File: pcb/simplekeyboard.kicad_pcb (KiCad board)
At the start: 2 copper layers, 288.1 x 97.6 mm, 164 parts, among them J1 USB_C_Receptacle_USB2.0_16P, J2 Conn_ARM_JTAG_SWD_10, SW1 SW_Push, SW10 SW_Push, SW11 SW_Push, SW12 SW_Push, SW13 SW_Push, SW14 SW_Push, SW15 SW_Push, SW16 SW_Push, SW17 SW_Push, SW18 SW_Push, SW19 SW_Push, SW2 SW_Push, SW20 SW_Push, SW21 SW_Push, SW22 SW_Push, SW23 SW_Push, SW24 SW_Push, SW25 SW_Push, SW26 SW_Push, SW27 SW_Push, SW28 SW_Push, SW29 SW_Push, SW3 SW_Push, SW30 SW_Push, SW31 SW_Push, SW32 SW_Push, SW33 SW_Push, SW34 SW_Push, SW35 SW_Push, SW36 SW_Push, SW37 SW_Push, SW38 SW_Push, SW39 SW_Push, SW4 SW_Push, SW40 SW_Push, SW41 SW_Push, SW42 SW_Push, SW43 SW_Push, SW44 SW_Push, SW45 SW_Push, SW46 SW_Push, SW47 SW_Push, SW48 SW_Push, SW49 SW_Push, SW5 SW_Push, SW50 SW_Push, SW51 SW_Push, SW52 SW_Push, SW53 SW_Push, SW54 SW_Push, SW55 SW_Push, SW56 SW_Push, SW57 SW_Push, SW58 SW_Push, SW59 SW_Push, SW6 SW_Push, SW60 SW_Push, SW61 SW_Push, SW62 SW_SPDT, SW63 SW_Push, SW7 SW_Push, SW8 SW_Push, SW9 SW_Push, U1 STM32F072CBT6, U2 USBLC6-2SC6, U3 LD39050PU33R, U4 MCP23017_SO, U5 MCP23008-xSO

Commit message: Cleanup silkscreen
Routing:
- net GND: track 65.4 -> 68.7 mm, vias 88 -> 91
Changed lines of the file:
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@@
 			(at 0 -4.5 0)
 			(layer "F.SilkS")
+			(hide yes)
 			(effects
 				(font
@@
 		)
 		(fp_text user "${REFERENCE}"
+			(at 0 -4.75 0)
+			(layer "F.Fab")
+			(effects
+				(font
+					(size 1 1)
+					(thickness 0.15)
+				)
+			)
+		)
+		(fp_text user "${REFERENCE}"
 			(at 0 0 0)
 			(layer "F.Fab")
@@
 			(at 0 -3.5 0)
 			(layer "F.SilkS")
+			(hide yes)
 			(effects
 				(font
@@
 			(at 0 -3.5 0)
 			(layer "F.SilkS")
+			(hide yes)
 			(effects
 				(font
@@
 			(at 0 -4.5 0)
 			(layer "F.SilkS")
+			(hide yes)
 			(effects
 				(font
@@
 			(at 0 -4.5 0)
 			(layer "F.SilkS")
+			(hide yes)
 			(effects
 				(font
@@
 			(at 0 -4.5 0)
 			(layer "F.SilkS")
+			(hide yes)
 			(effects
 				(font
@@
 		(tags "capacitor")
 		(property "Reference" "C7"
-			(at 0 1.43 0)
+			(at 0 -1.6 0)
 			(layer "B.SilkS")
 			(effects
@@
 		(tags "resistor")
 		(property "Reference" "R1"
-			(at 0 1.65 180)
+			(at -2.6 0 180)
 			(layer "B.SilkS")
 			(effects
@@
 		(tags "capacitor")
 		(property "Reference" "C2"
-			(at 0 1.43 0)
+			(at -0.6 1.4 0)
 			(layer "B.SilkS")
 			(effects
@@
 		(tags "capacitor")
 		(property "Reference" "C9"
-			(at 0 1.43 0)
+			(at 0 -1.4 0)
 			(layer "B.SilkS")
 			(effects
@@
 		(tags "capacitor")
 		(property "Reference" "C13"
-			(at 0 1.43 90)
+			(at -3.05 0 90)
 			(layer "B.SilkS")
 			(effects
@@
 		(tags "capacitor")
 		(property "Reference" "C12"
-			(at 0 1.43 90)
+			(at -3.05 0 90)
 			(layer "B.SilkS")
 			(effects
@@
 		(tags "capacitor")
 		(property "Reference" "C10"
-			(at 0 1.43 0)
+			(at 0.7 1.43 0)
 			(layer "B.SilkS")
 			(effects
@@
 		(tags "LD39050PU33R ")
 		(property "Reference" "U3"
-			(at 0 -2.600001 270)
+			(at -0.540625 -2.878125 0)
 			(unlocked yes)
 			(layer "B.SilkS")
@@
 		(tags "SOD-123")
 		(property "Reference" "D62"
-			(at 0 -1.85 0)
+			(at 0 1.6875 0)
 			(layer "B.SilkS")
 			(effects
@@
 		(tags "SOT TO_SOT_SMD")
 		(property "Reference" "U2"
-			(at 0 2.4 90)
+			(at 0 -2.578125 90)
 			(layer "B.SilkS")
 			(effects
@@
 		(tags "capacitor")
 		(property "Reference" "C8"
-			(at 0 1.43 0)
+			(at 0 -1.4 0)
 			(layer "B.SilkS")
 			(effects
@@
 		(tags "resistor")
 		(property "Reference" "R7"
-			(at 0 1.43 0)
+			(at -2.4 0 0)
 			(layer "B.SilkS")
 			(effects
@@
 		(tags "resistor")
 		(property "Reference" "R5"
-			(at 0 1.43 90)
+			(at -2.6 0 90)
 			(layer "B.SilkS")
 			(effects
@@
 		(tags "SOD-123")
 		(property "Reference" "D29"
-			(at 0 2 90)
+			(at 0 -1.8 90)
 			(layer "B.SilkS")
 			(effects
@@
 		(tags "resistor")
 		(property "Reference" "R2"
-			(at 0 1.65 180)
+			(at -2.6 0 180)
 			(layer "B.SilkS")
 			(effects
@@
 		(tags "resistor")
 		(property "Reference" "R10"
-			(at 0 1.43 90)
+			(at -3.05 0 90)
 			(layer "B.SilkS")
 			(effects
@@
 		(tags "resistor")
 		(property "Reference" "R9"
-			(at 0 1.43 90)
+			(at -2.6 0 90)
 			(layer "B.SilkS")
 			(effects
@@
 		(tags "resistor")
 		(property "Reference" "R4"
-			(at 0 1.43 90)
+			(at -2.6 0 90)
 			(layer "B.SilkS")
 			(effects
@@
 		(tags "resistor")
 		(property "Reference" "R8"
-			(at 0 1.43 90)
+			(at 0 -1.4 90)
 			(layer "B.SilkS")
 			(effects
@@
 	)
 	(via
+		(at 60.134375 43.384375)
+		(size 0.8)
+		(drill 0.3)
+		(layers "F.Cu" "B.Cu")
+		(net 2)
+	)
+	(via
 		(at 207.16875 78.58125)
 		(size 0.8)
@@
 	)
 	(via
+		(at 50.884375 37.134375)
+		(size 0.8)
+		(drill 0.3)
+		(layers "F.Cu" "B.Cu")
+		(free yes)
+		(net 2)
+	)
+	(via
 		(at 202.40625 59.53125)
 		(size 0.8)
@@
 	)
 	(via
+		(at 60.134375 41.384375)
+		(size 0.8)
+		(drill 0.3)
+		(layers "F.Cu" "B.Cu")
+		(net 2)
+	)
+	(via
 		(at 40.584375 46.784375)
 		(size 0.8)
@@
 	)
 	(segment
+		(start 58.496875 43.384375)
+		(end 60.134375 43.384375)
+		(width 0.4)
+		(layer "B.Cu")
+		(net 2)
+	)
+	(segment
 		(start 53.184375 68.384375)
 		(end 52.796875 67.996875)
@@
 		(width 0.4)
 		(layer "B.Cu")
+		(net 2)
+	)
+	(segment
+		(start 58.496875 41.384375)
+		(end 60.134375 41.384375)
+		(width 0.4)
+		(layer "B.Cu")

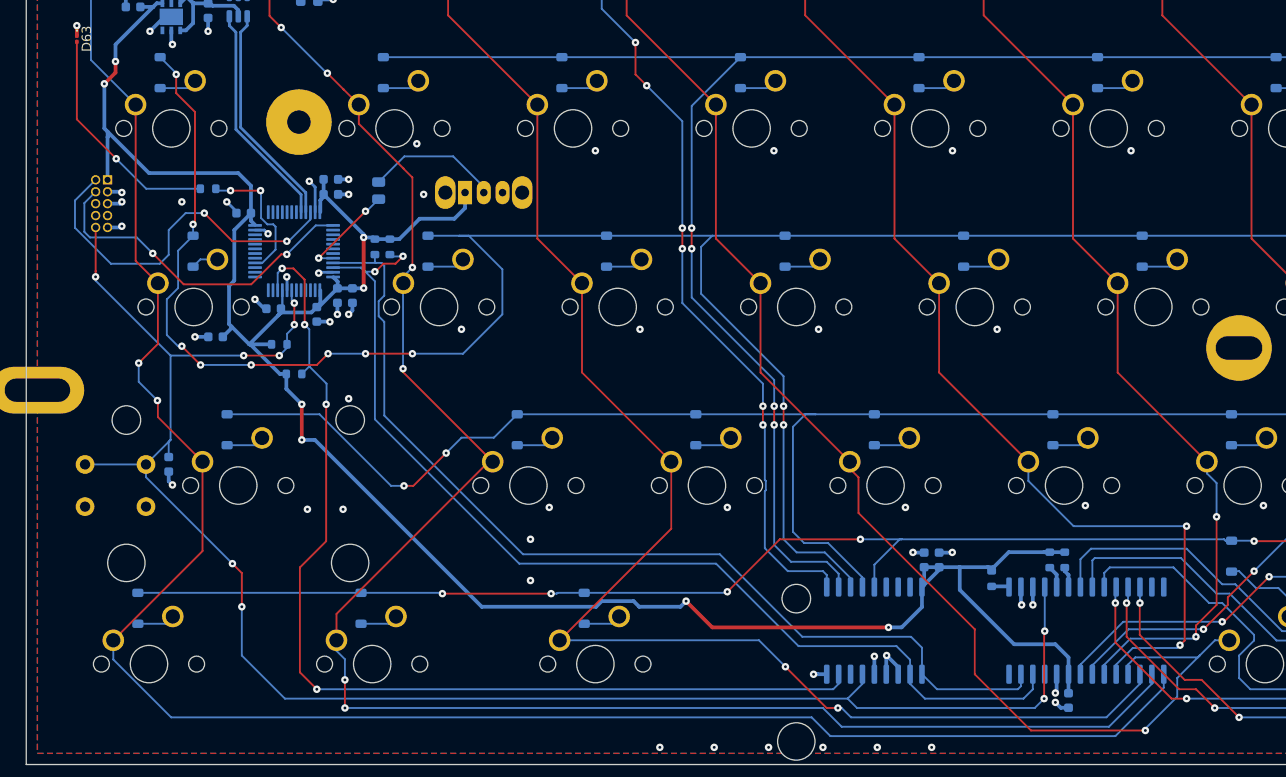
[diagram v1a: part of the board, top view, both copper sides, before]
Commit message: Fixed critical mistake where CAPSLOCK and Tab were indistinguishable
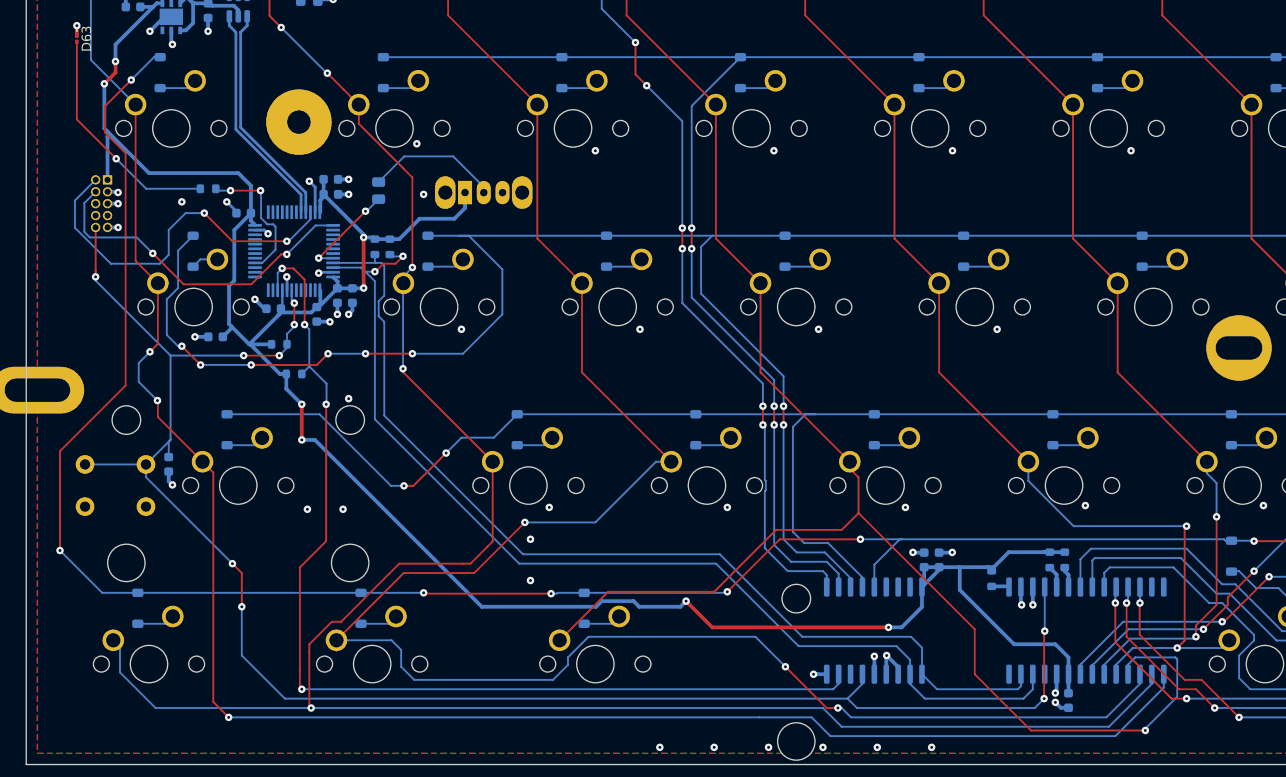
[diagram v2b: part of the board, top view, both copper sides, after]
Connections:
- D15 pad 2: /ROW2 -> /ROW4
- SW54 pad 1: /Matrix/COL0 -> /Matrix/COL1
- SW55 pad 1: /Matrix/COL1 -> /Matrix/COL2
- SW56 pad 1: /Matrix/COL2 -> /Matrix/COL3
- SW57 pad 1: /Matrix/COL3 -> /Matrix/COL4
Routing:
- net /ROW4: track 275.2 -> 344.7 mm, vias 6 -> 8
- net /Matrix/COL2: track 158.8 -> 208.7 mm, vias 2 -> 3
- net /Matrix/COL1: track 191.5 -> 226.9 mm, vias 6 -> 5
- net /Matrix/COL3: track 139.2 -> 169.1 mm
- net /ROW2: track 352.5 -> 331.9 mm, vias 10 -> 8
- net /Matrix/COL0: track 207.9 -> 196.4 mm, vias 2 -> 3
- net /Matrix/COL4: track 109.6 -> 115.5 mm
- net GND: track 68.7 -> 67.4 mm
- net /ROW_INT: track 110.1 -> 111.0 mm

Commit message: Changed a few footrpints
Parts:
- C10, C11, C13, C14, C3, C4, C5, C8: footprint Capacitor_SMD:C_0603_1608Metric -> Capacitor_SMD:C_0402_1005Metric
- D63: footprint LED_SMD:LED_0201_0603Metric -> LED_SMD:LED_0603_1608Metric
- H5, H6: footprint Keyboard_Mounts:2.5mm_Wide -> Keyboard_Mounts:2.5mm_Oblong
- R1, R2, R3: footprint Resistor_SMD:R_0805_2012Metric -> Resistor_SMD:R_0603_1608Metric
- moved H5 3.69 mm to (32.3, 85.1)
- moved H6 2.94 mm to (310.6, 85.1)
- moved C9 1.78 mm to (61.0, 64.0)
- moved C10 1.30 mm to (60.4, 65.4)
- moved C3 0.57 mm to (58.8, 76.6)
- moved C8 0.45 mm to (54.2, 76.2)
- moved C5 0.45 mm to (60.8, 74.6)
- moved R2 0.40 mm to (57.6, 43.0)
- moved C13 0.40 mm to (123.2, 103.6)
- moved C4 0.20 mm to (50.6, 66.4)
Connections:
- net /SWIO renamed /SWDIO
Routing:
- net GND: track 67.4 -> 63.9 mm
- net +3.3V: track 249.7 -> 246.7 mm
- removed copper zone on B.Cu, net GND

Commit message: Back pour deleted by mistake
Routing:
- added copper zone on B.Cu, net GND
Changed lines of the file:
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@@
+		)
+	)
+	(zone
+		(net 2)
+		(net_name "GND")
+		(locked yes)
+		(layer "B.Cu")
+		(hatch edge 0.5)
+		(connect_pads
+			(clearance 0.5)
+		)
+		(min_thickness 0.25)
+		(filled_areas_thickness no)
+		(fill yes
+			(thermal_gap 0.5)
+			(thermal_bridge_width 0.5)
+		)
+		(polygon
+			(pts
+				(xy 28.575 28.575) (xy 28.575 123.825) (xy 314.325 123.825) (xy 314.325 28.575)
+			)
 		)
 	)

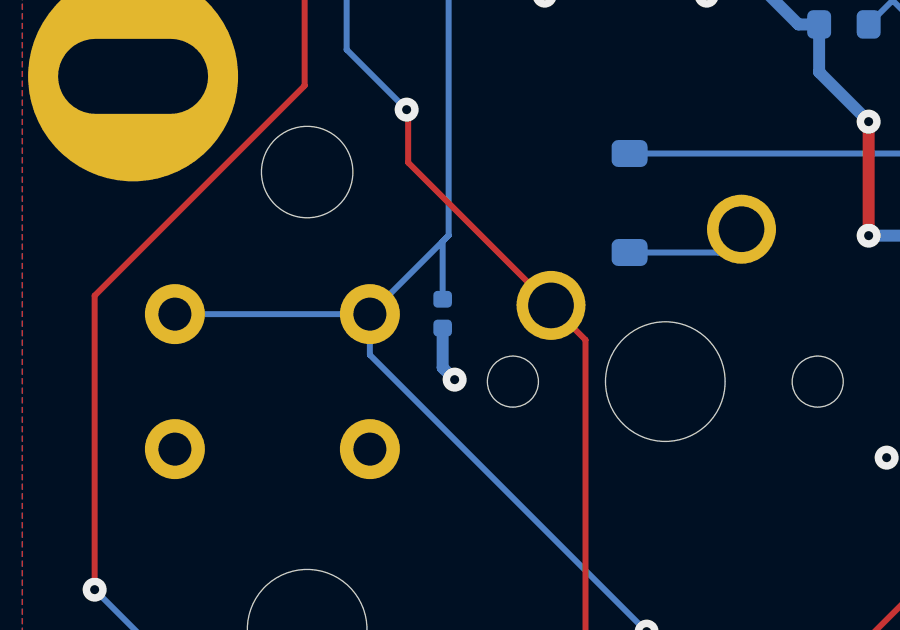
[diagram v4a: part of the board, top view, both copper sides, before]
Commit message: Moved cap
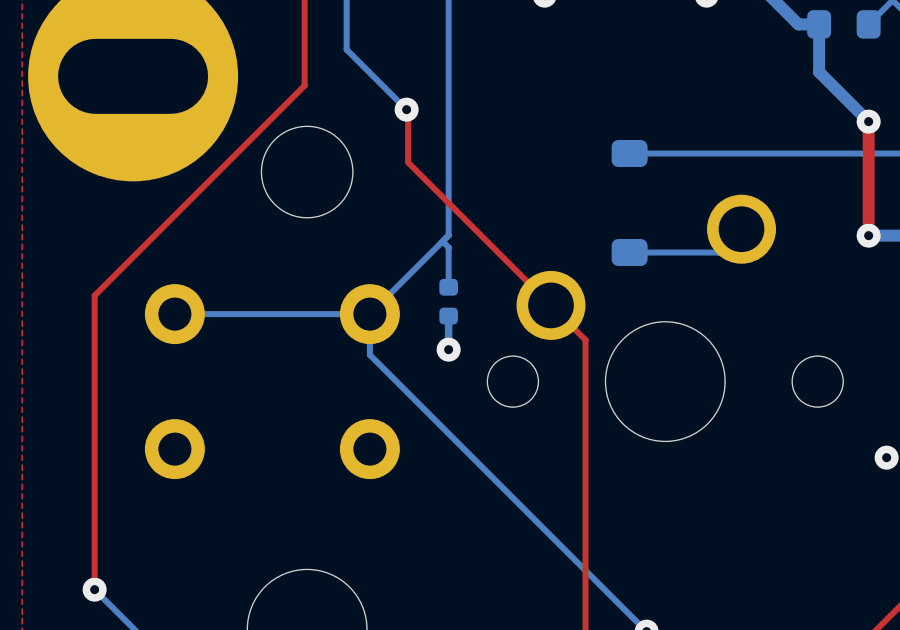
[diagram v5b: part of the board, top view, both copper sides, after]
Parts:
- moved C11 0.45 mm to (42.8, 92.6)
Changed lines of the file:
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@@
 	(footprint "Capacitor_SMD:C_0402_1005Metric"
 		(layer "B.Cu")
-		(at 42.584375 92.984375 90)
+		(at 42.784375 92.584375 90)
 		(descr "Capacitor SMD 0402 (1005 Metric), square (rectangular) end terminal, IPC_7351 nominal, (Body size source: IPC-SM-782 page 76, https://www.pcb-3d.com/wordpress/wp-content/uploads/ipc-sm-782a_amendment_1_and_2.pdf), generated with kicad-footprint-generator")
 		(tags "capacitor")
@@
 	)
 	(via
-		(at 42.984375 95.184375)
-		(size 0.8)
-		(drill 0.3)
-		(layers "F.Cu" "B.Cu")
-		(net 2)
-	)
-	(via
 		(at 178.384375 97.384375)
 		(size 0.8)
@@
 	)
 	(via
+		(at 42.784375 94.184375)
+		(size 0.8)
+		(drill 0.3)
+		(layers "F.Cu" "B.Cu")
+		(net 2)
+	)
+	(via
 		(at 221.45625 59.53125)
 		(size 0.8)
@@
 	)
 	(segment
-		(start 42.584375 94.784375)
-		(end 42.984375 95.184375)
-		(width 0.4)
-		(layer "B.Cu")
-		(net 2)
-	)
-	(segment
 		(start 37.184375 67.714375)
 		(end 36.059375 67.714375)
@@
 	)
 	(segment
+		(start 42.784375 93.064375)
+		(end 42.784375 94.184375)
+		(width 0.25)
+		(layer "B.Cu")
+		(net 2)
+	)
+	(segment
 		(start 50.104375 66.384375)
 		(end 48.984375 66.384375)
@@
 	)
 	(segment
-		(start 42.584375 93.759375)
-		(end 42.584375 94.784375)
-		(width 0.4)
-		(layer "B.Cu")
-		(net 2)
-	)
-	(segment
 		(start 36.909375 50.00625)
 		(end 36.909375 51.196875)
@@
 	)
 	(segment
+		(start 42.584375 90.575)
+		(end 42.784375 90.775)
+		(width 0.2)
+		(layer "B.Cu")
+		(net 4)
+	)
+	(segment
 		(start 33.659375 93)
 		(end 40.159375 93)
@@
 	)
 	(segment
+		(start 42.784375 90.775)
+		(end 42.784375 92.104375)
+		(width 0.2)
+		(layer "B.Cu")
+		(net 4)
+	)
+	(segment
 		(start 116.020624 118.984375)
 		(end 134.984375 118.984375)
@@
 		(width 0.2)
 		(layer "B.Cu")
-		(net 4)
-	)
-	(segment
-		(start 42.584375 90.575)
-		(end 42.584375 92.209375)
-		(width 0.2)
-		(layer "B.Cu")
